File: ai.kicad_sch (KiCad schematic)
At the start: 8 parts, among them U18 TS912

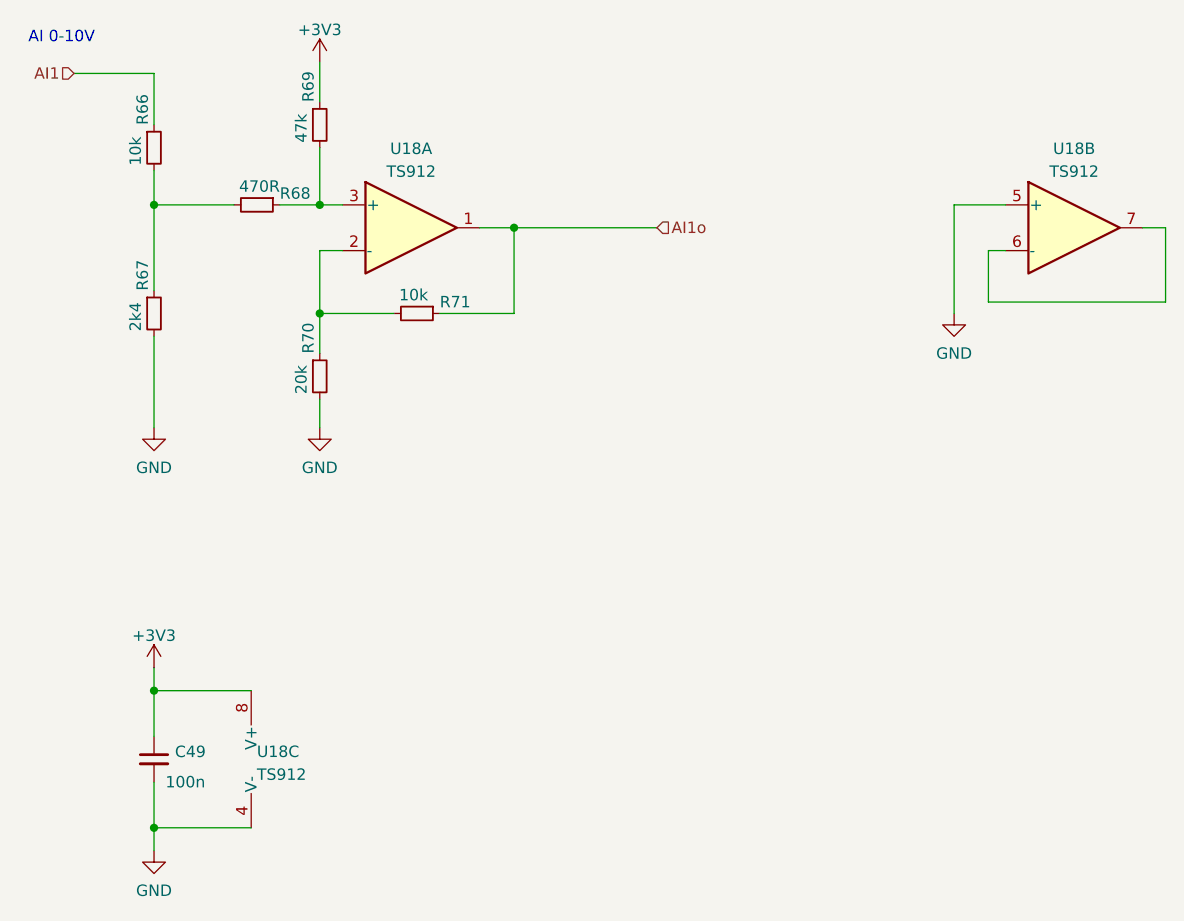
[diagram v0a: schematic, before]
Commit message: Layout optimized
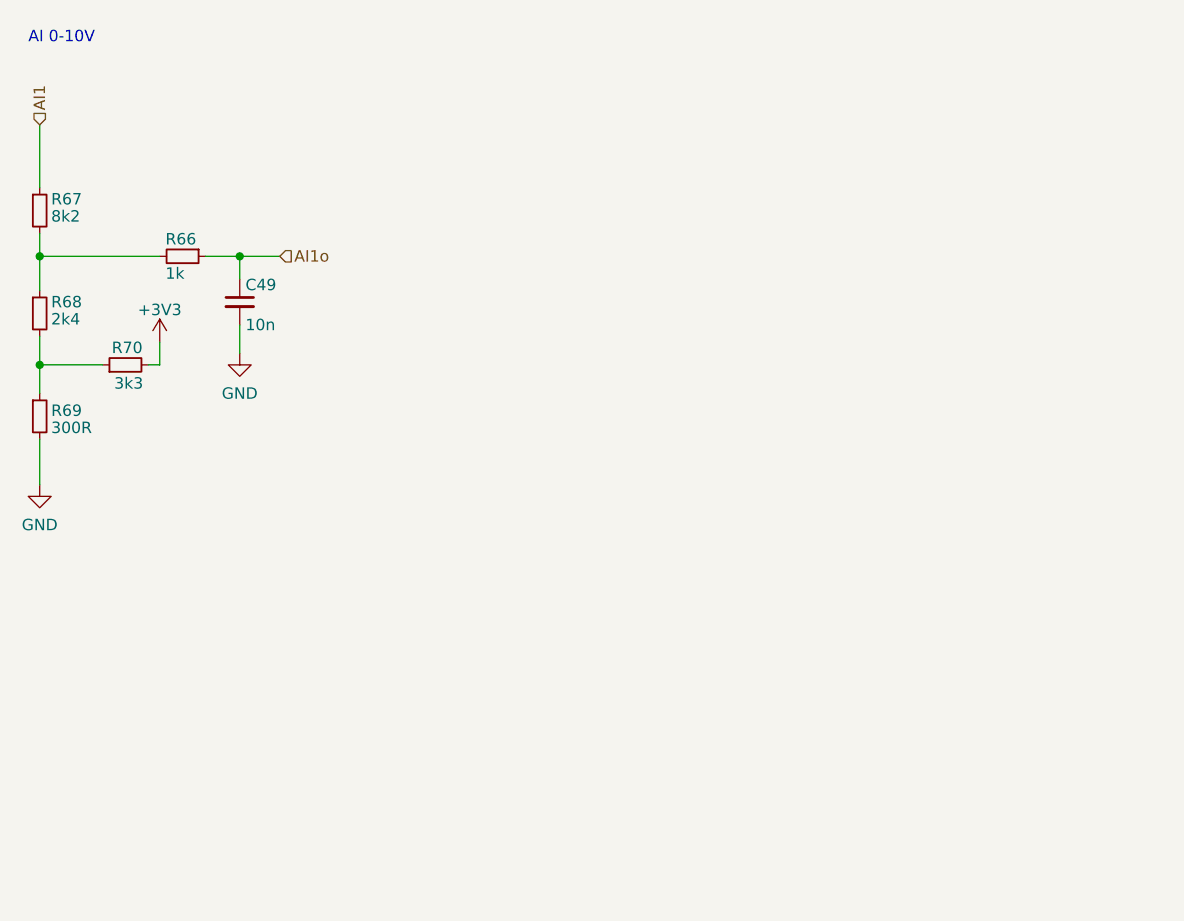
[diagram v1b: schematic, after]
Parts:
- removed R71: 10k, Resistor_SMD:R_0603_1608Metric, symbol Device:R_Small
- removed U18: TS912, Package_SO:SO-8_3.9x4.9mm_P1.27mm, symbol Amplifier_Operational:TS912
- C49: value 100n -> 10n
- R66: value 10k -> 1k
- R67: value 2k4 -> 8k2
- R68: value 470R -> 2k4
- R69: value 47k -> 300R
- R70: value 20k -> 3k3
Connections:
- net +3V3: now also R70.2; no longer C49.1, R69.1
- net AI1: now also R67.1; no longer R66.1
- net AI1o: now also C49.1, R66.1
- net GND: now also R69.2; no longer R67.2, R70.2
- net at R70.1: now also R68.2, R69.1
- net at R68.1: now also R66.2, R67.2; no longer R69.2
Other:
- moved on the sheet: C49, R66, R67, R68, R69, R70
